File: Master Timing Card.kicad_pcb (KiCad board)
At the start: 4 copper layers, 170 x 100 mm, 246 parts, among them CN1 Pin_03, CN2 Samtec GRF1-J-P-08-E-RA-TH1, CN3 Amphenol 86093488613755E1LF, CN6 SQW-104-01-F-D-VS, CN7 104031-0811, CN8 104031-0811, J1 Connector_RJ45_Magjack_Abraco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, Q1 DMN62D0U-7, Q2 DMN62D0U-7, Q3 DMN62D0U-7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

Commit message: .
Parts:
- moved C119 201.2 mm to (63.7, 38.8), turned to 90 degrees
- moved R16 198.5 mm to (63.7, 41.6), turned to 90 degrees
- moved R17 196.4 mm to (65.7, 41.6), turned to 90 degrees
- moved R18 194.2 mm to (67.7, 41.6), turned to 90 degrees
- moved C120 194.1 mm to (63.7, 46.5), turned to 90 degrees
- moved R19 192.1 mm to (69.7, 41.6), turned to 90 degrees
- moved C121 192.0 mm to (65.7, 46.5), turned to 90 degrees
- moved R52 191.6 mm to (63.7, 49.4), turned to 90 degrees
- moved C122 189.8 mm to (67.7, 46.5), turned to 90 degrees
- moved T1 189.6 mm to (85.0, 72.5), turned to 180 degrees
- moved R53 189.4 mm to (65.7, 49.4), turned to 90 degrees
- moved D2 188.2 mm to (74.2, 40.9), turned to 90 degrees
- moved R54 187.2 mm to (67.7, 49.4), turned to 90 degrees
- moved T2 186.0 mm to (90.0, 72.5), turned to 180 degrees
- moved C27 185.8 mm to (83.8, 76.5), turned to 90 degrees
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
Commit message: Added M.2 SSD
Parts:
- added CN10: M2 x 2.5mm, Connector_WUT:Standoff_Wurth_9774025243R, F.Cu at (157.8, 54.5)
- added CN9: TE 1-2199230-6, Connector_WUT:TE_1-2199230-6, F.Cu at (115.8, 54.5)
- moved R56 442.4 mm to (513.2, 20.7)
- moved C119 442.4 mm to (505.2, 10.0)
- moved C120 442.4 mm to (505.2, 17.8)
- moved C121 442.4 mm to (507.2, 17.8)
- moved C122 442.4 mm to (509.2, 17.8)
- moved LD1 442.4 mm to (522.9, 30.5)
- moved R16 442.4 mm to (505.2, 12.9)
- moved R17 442.4 mm to (507.2, 12.9)
- moved R18 442.4 mm to (509.2, 12.9)
- moved R19 442.4 mm to (511.2, 12.9)
- moved R52 442.4 mm to (505.2, 20.7)
- moved R53 442.4 mm to (507.2, 20.7)
- moved R54 442.4 mm to (509.2, 20.7)
- moved R55 442.4 mm to (511.2, 20.7)
- moved U8 442.4 mm to (522.5, 19.6)
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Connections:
- CN5 pad 110: unconnected-(CN5A-PCIe_CLK_P-Pad110) -> /Pi CM4 - HPIO/PCIE_REFCLK_P
- CN5 pad 112: unconnected-(CN5A-PCIe_CLK_N-Pad112) -> /Pi CM4 - HPIO/PCIE_REFCLK_N
- CN5 pad 116: unconnected-(CN5A-PCIe_RX_P-Pad116) -> /Pi CM4 - HPIO/PCIE_PER0_P
- CN5 pad 118: unconnected-(CN5A-PCIe_RX_N-Pad118) -> /Pi CM4 - HPIO/PCIE_PER0_N
- CN5 pad 122: unconnected-(CN5A-PCIe_TX_P-Pad122) -> /Pi CM4 - HPIO/PCIE_PET0_P
- CN5 pad 124: unconnected-(CN5A-PCIe_TX_N-Pad124) -> /Pi CM4 - HPIO/PCIE_PET0_N

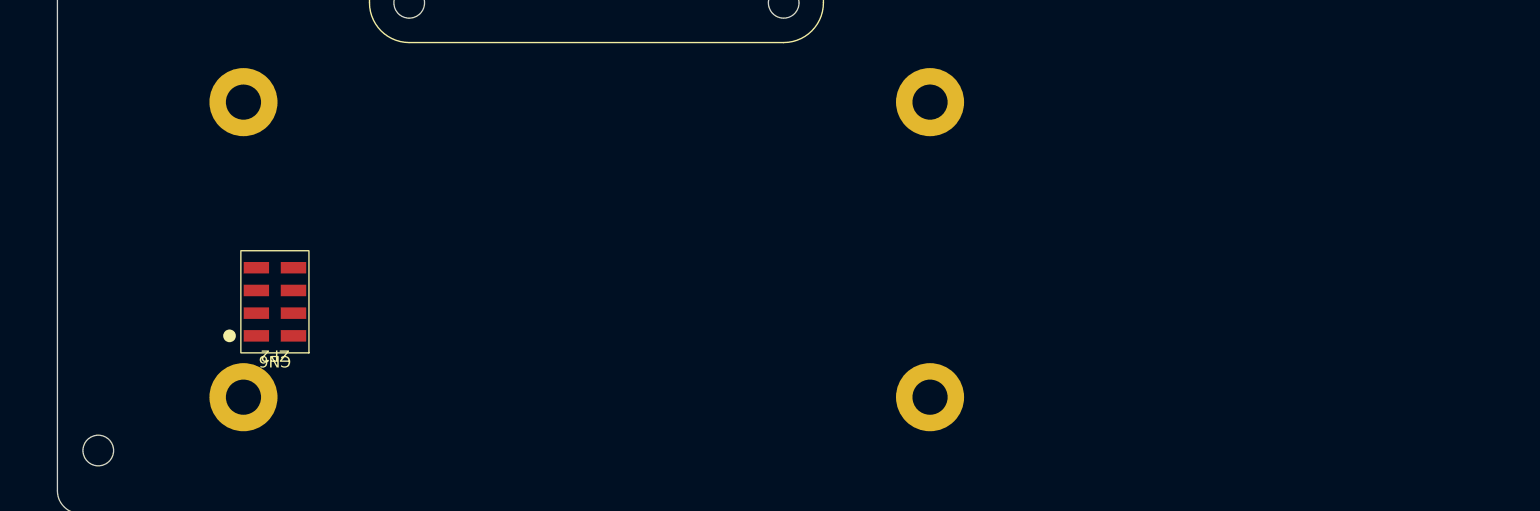
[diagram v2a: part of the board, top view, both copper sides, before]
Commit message: Added SFP connector
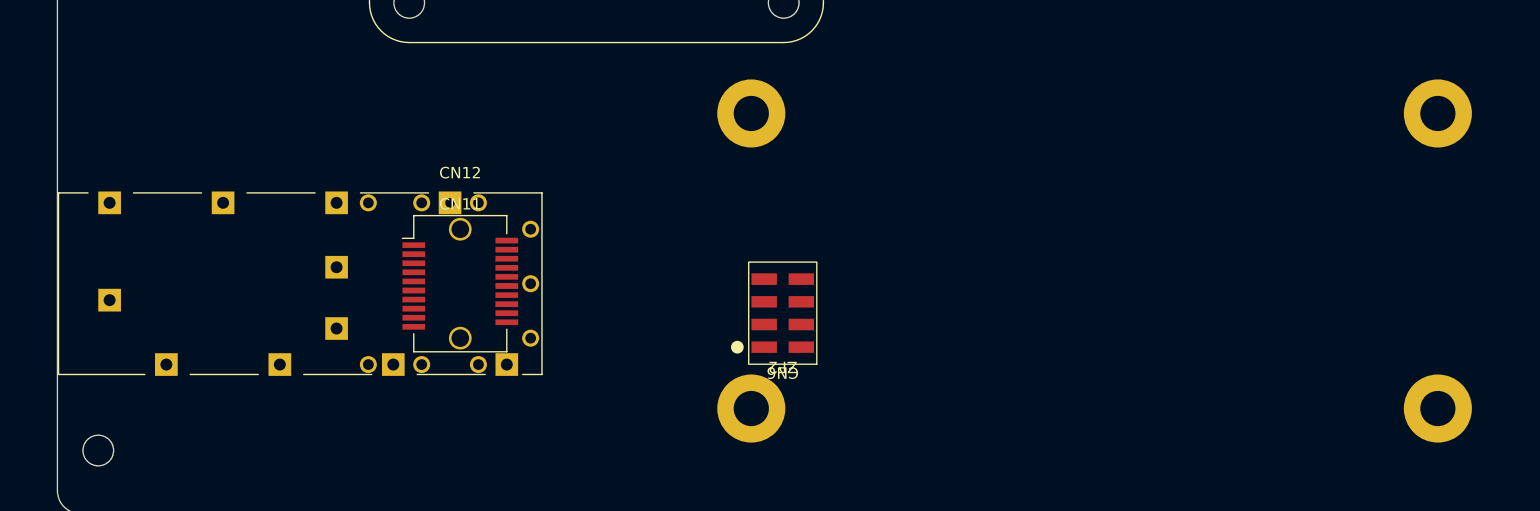
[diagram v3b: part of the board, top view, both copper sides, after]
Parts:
- added CN11: UE75-A20-6000T, Connector_WUT:Amphenol_UE75-A20-6000T, F.Cu at (75.5, 104.8)
- added CN12: U77-A1114-30L1, Connector_WUT:Amphenol_U77-A1114-30L1, F.Cu at (75.5, 104.8)
- moved CN6 44.8 mm to (103.9, 107.3)
- moved ZF2 44.8 mm to (103.9, 107.3)
